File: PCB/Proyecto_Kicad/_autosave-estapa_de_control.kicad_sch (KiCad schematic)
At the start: 68 parts, among them K1 SANYOU_SRD_Form_C, K2 SANYOU_SRD_Form_C, K3 SANYOU_SRD_Form_C, Q1 BC548, Q10 BC548, Q11 BC548, Q12 BC548, Q13 BC548, Q2 BC548, Q3 BC548, Q4 BC548, Q5 BC548, Q6 BC548, Q7 BC548, Q8 BC548, Q9 BC548, U1 ESP-01v090, U2 RP2040-Zero

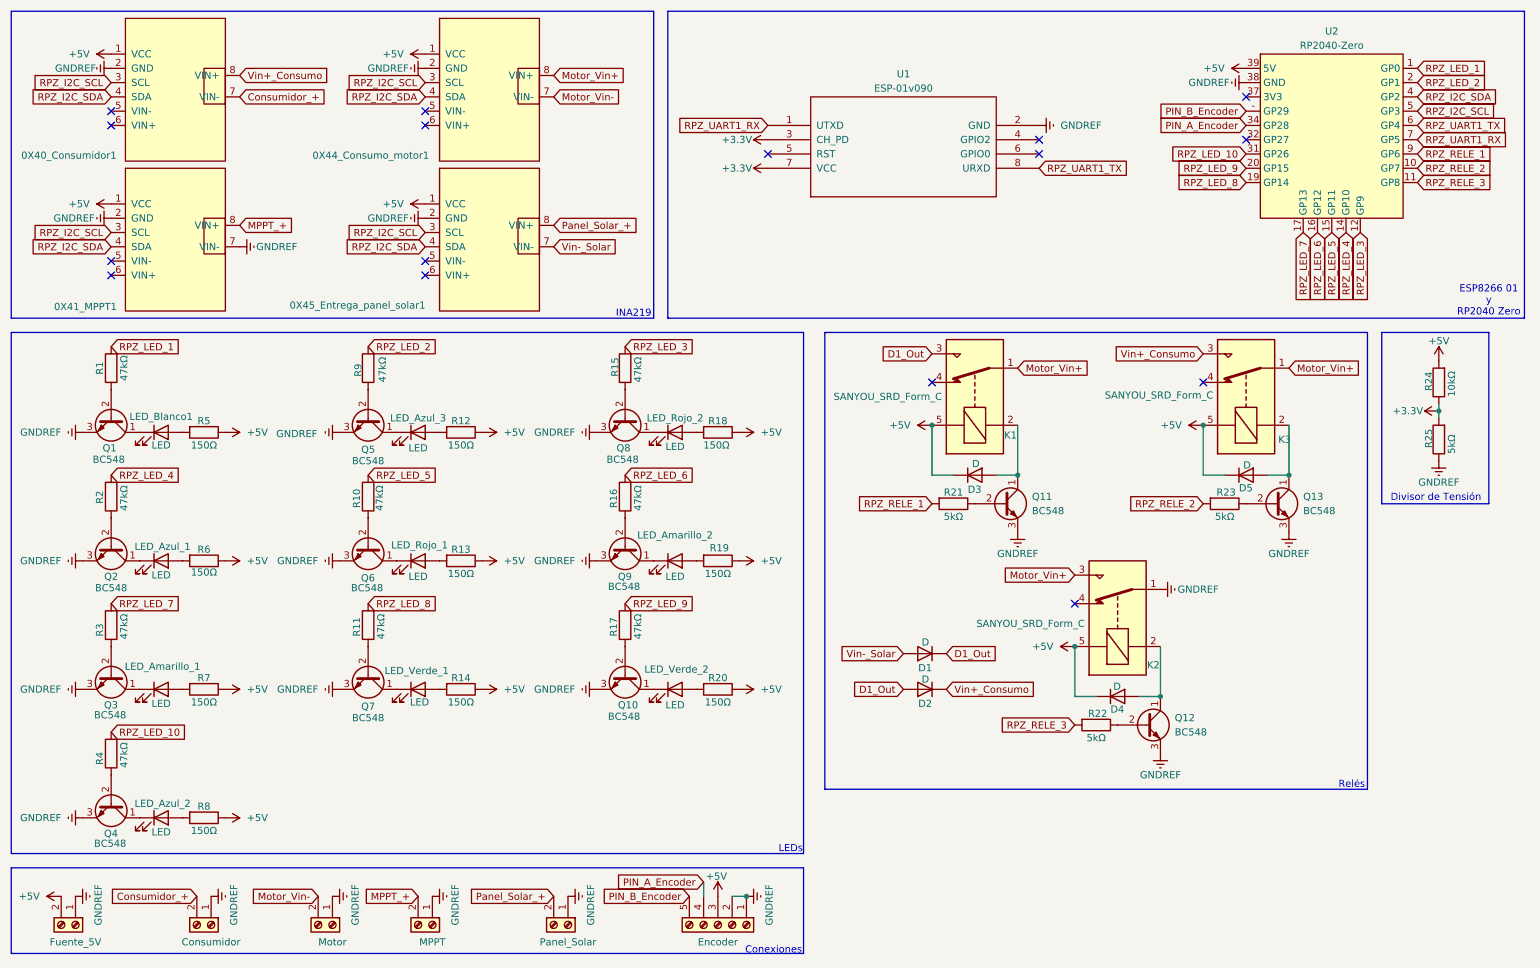
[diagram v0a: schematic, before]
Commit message: fix: "Corrección de errores de la placa"
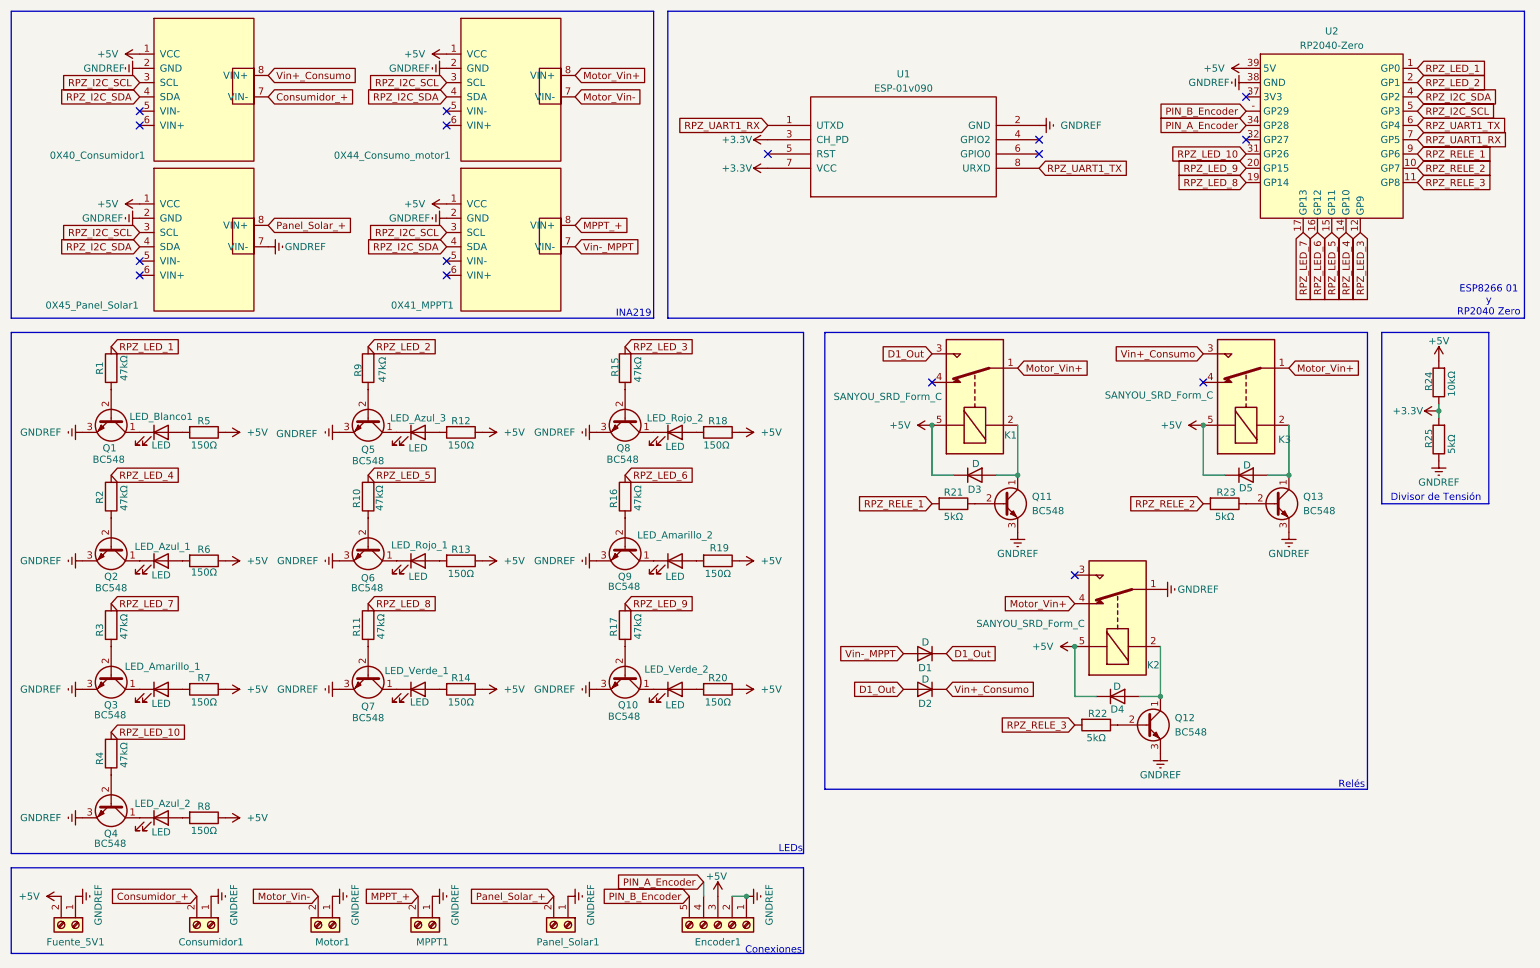
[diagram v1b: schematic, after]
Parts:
- renumbered 0X45_Entrega_panel_solar1 to 0X41_MPPT1, 0X41_MPPT1 to 0X45_Panel_Solar1, Consumidor to Consumidor1, Encoder to Encoder1, Fuente_5V to Fuente_5V1, MPPT to MPPT1, Motor to Motor1, Panel_Solar to Panel_Solar1
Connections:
- net MPPT_+: now also 0X41_MPPT1.8 (VIN+); no longer 0X45_Panel_Solar1.8 (VIN+)
- net Motor_Vin+: now also K2.4; no longer K2.3
- net Panel_Solar_+: now also 0X45_Panel_Solar1.8 (VIN+); no longer 0X41_MPPT1.8 (VIN+)
- net Vin-_Solar renamed Vin-_MPPT
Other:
- moved on the sheet: 0X40_Consumidor1, 0X41_MPPT1, 0X44_Consumo_motor1, 0X45_Panel_Solar1
